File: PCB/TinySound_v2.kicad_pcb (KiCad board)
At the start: 4 copper layers, 15.2 x 20 mm, 35 parts, among them J1 Conn_01x07, J2 USB_B_Micro, J3 Conn_01x07, U1 MIC5504-3.3YMT, U2 MAX98360AEFB+T, U3 RP2040, U4 W25Q128JVS, Y1 12M

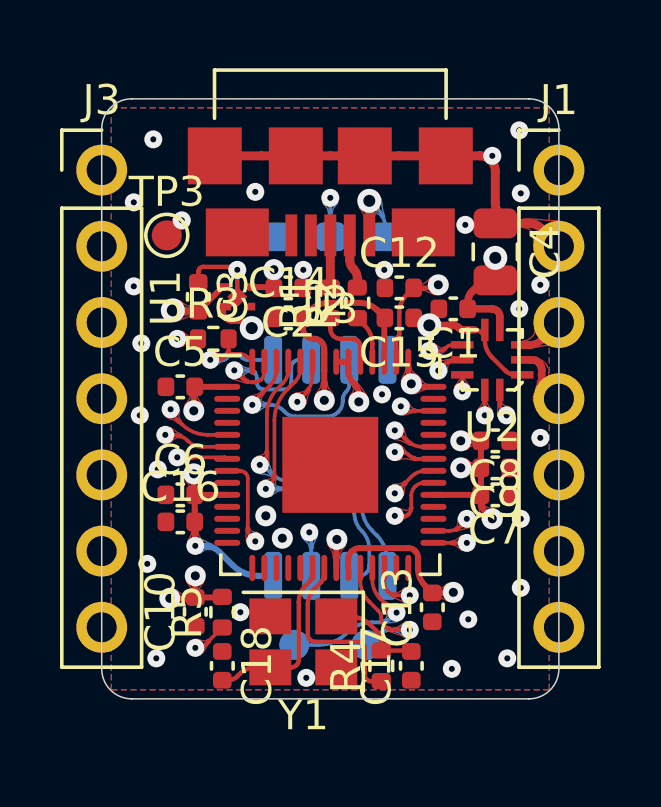
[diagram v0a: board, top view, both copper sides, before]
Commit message: Cleared round traces on PCB, added WS2812 in schematic
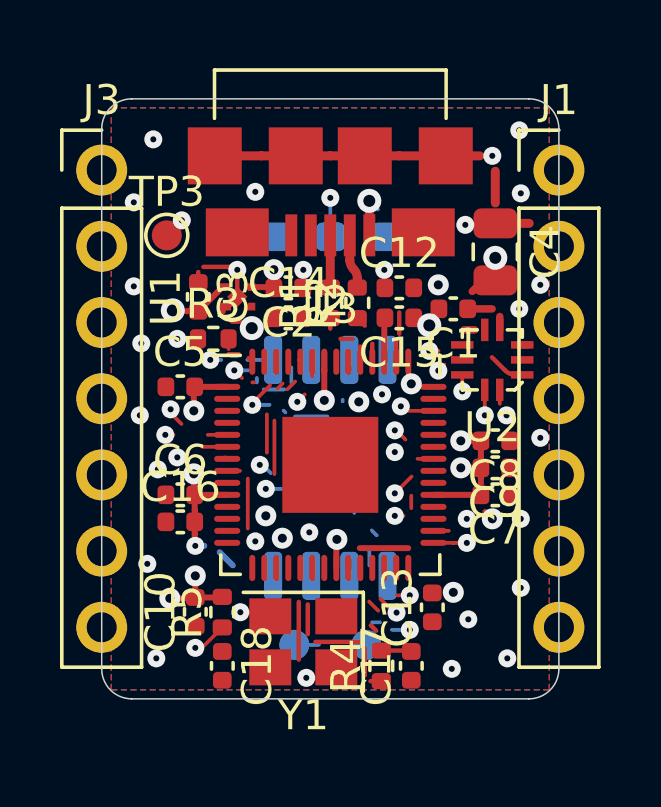
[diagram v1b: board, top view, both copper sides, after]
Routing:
- net +3V3: track 75.3 -> 55.3 mm
- net /+1V1: track 21.1 -> 10.00 mm
- net GND: track 23.2 -> 15.8 mm
- net +5V: track 21.7 -> 14.6 mm
- net /GPIO4: track 11.0 -> 5.33 mm
- net /QSPI_SD0: track 10.4 -> 4.84 mm
- net /RUN: track 14.1 -> 9.32 mm
- net /QSPI_SCLK: track 10.9 -> 6.21 mm
- net /AU_DIN: track 8.66 -> 4.56 mm
- net /QSPI_SD2: track 6.57 -> 2.89 mm
- net /SWCLK: track 4.67 -> 1.03 mm
- net /SWDIO: track 5.53 -> 1.91 mm
- net /AU_GAIN: track 9.55 -> 6.37 mm
- net /BOOTSEL: track 6.27 -> 3.19 mm
- net /QSPI_SD3: track 7.46 -> 4.50 mm
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
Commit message: New component arrangement vor v2.1
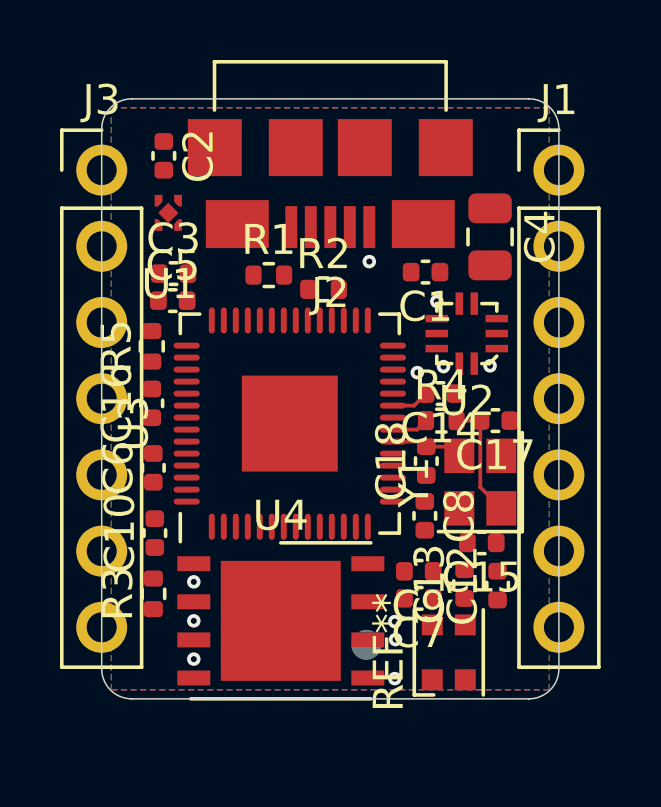
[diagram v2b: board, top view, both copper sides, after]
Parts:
- removed R6, R7: 100k, Resistor_SMD:R_0603_1608Metric_Pad0.98x0.95mm_HandSolder
- removed TP3: TestPoint, TestPoint:TestPoint_Pad_D1.0mm
- added REF**: LED_WS2812B-2020_PLCC4_2.0x2.0mm, LED_SMD:LED_WS2812B-2020_PLCC4_2.0x2.0mm, F.Cu at (104.0, 120.0)
- U4: footprint Package_SO:SOIC-8_5.23x5.23mm_P1.27mm -> Package_DFN_QFN:DFN-8-1EP_6x5mm_P1.27mm_EP4x4mm; moved to F.Cu
- Y1: footprint Crystal:Crystal_SMD_3225-4Pin_3.2x2.5mm -> Crystal:Crystal_SMD_2520-4Pin_2.5x2.0mm
- moved C12 10.5 mm to (105.6, 117.7), turned to 90 degrees
- moved C18 9.63 mm to (103.2, 113.6), turned to 90 degrees
- moved R5 9.17 mm to (94.0, 109.8)
- moved R3 8.73 mm to (94.1, 118.0), turned to 90 degrees
- moved C17 8.64 mm to (105.5, 112.2), turned to 180 degrees
- moved R4 8.42 mm to (103.7, 112.2), turned to 0 degrees
- moved C15 7.99 mm to (105.0, 116.3)
- moved Y1 7.95 mm to (105.0, 114.3), turned to 90 degrees
- moved C2 6.05 mm to (94.5, 103.4), turned to -90 degrees
- moved C14 5.67 mm to (103.7, 111.3), turned to 180 degrees
- moved U4 5.36 mm to (98.3, 118.9), turned to 0 degrees
- moved C7 4.29 mm to (103.0, 118.2)
- moved C9 4.29 mm to (103.0, 117.2)
- moved C16 4.06 mm to (94.0, 111.7), turned to 90 degrees
- moved U1 3.62 mm to (94.6, 105.3), turned to 0 degrees
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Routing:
- net +3V3: track 55.3 -> 0.00 mm, vias 13 -> 0
- net GND: track 15.8 -> 0.00 mm, vias 31 -> 7
- net +5V: track 14.6 -> 0.00 mm, vias 3 -> 0
- net /GPIO3: track 11.1 -> 0.00 mm, vias 1 -> 0
- net /RUN: track 9.32 -> 0.00 mm, vias 2 -> 0
- net /+1V1: track 10.00 -> 1.27 mm, vias 2 -> 1
- net /AU_GAIN: track 6.37 -> 0.00 mm, vias 2 -> 0
- net /QSPI_SCLK: track 6.21 -> 0.00 mm, vias 1 -> 0
- net /GPIO4: track 5.33 -> 0.00 mm, vias 1 -> 0
- net /AU_LRCLK: track 4.88 -> 0.00 mm, vias 2 -> 1
- net /QSPI_SD0: track 4.84 -> 0.00 mm, vias 1 -> 0
- net /AU_DIN: track 4.56 -> 0.00 mm, vias 2 -> 1
- net /QSPI_SD3: track 4.50 -> 0.00 mm, vias 2 -> 0
- net /AU_BCLK: track 4.16 -> 0.00 mm, vias 2 -> 0
- net /AU_EN: track 4.11 -> 0.00 mm, vias 2 -> 1
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
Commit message: Moved components to better positions
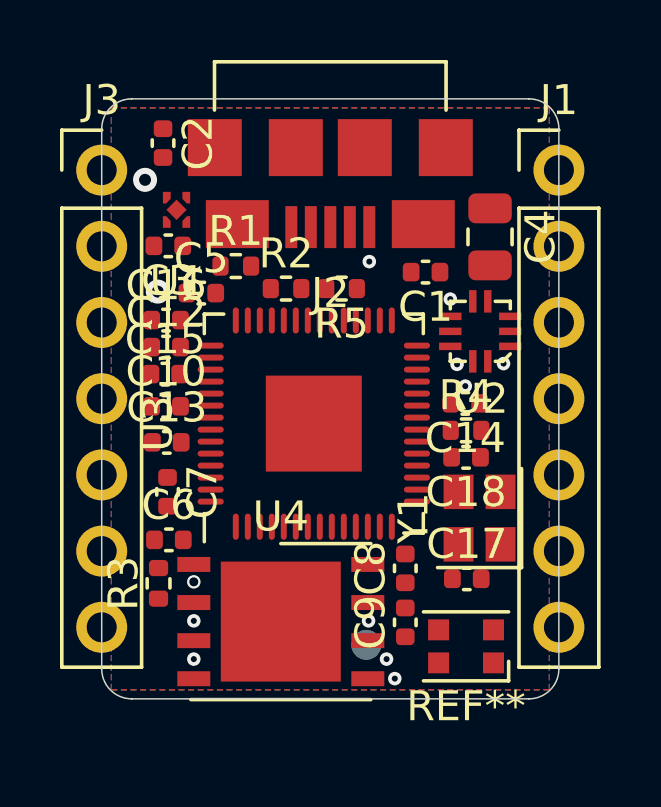
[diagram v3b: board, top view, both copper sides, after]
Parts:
- moved C12 13.6 mm to (94.5, 109.8), turned to 0 degrees
- moved C15 12.0 mm to (94.5, 110.7), turned to 0 degrees
- moved C13 11.0 mm to (94.5, 113.0), turned to 0 degrees
- moved C7 9.10 mm to (94.6, 114.6), turned to -90 degrees
- moved R5 6.61 mm to (100.4, 107.8), turned to 180 degrees
- moved C17 5.36 mm to (104.5, 117.5), turned to 0 degrees
- moved C10 4.24 mm to (94.5, 111.8), turned to 0 degrees
- moved C16 2.82 mm to (94.5, 108.9), turned to 0 degrees
- moved C6 2.46 mm to (94.6, 116.2), turned to 0 degrees
- moved C8 1.87 mm to (102.5, 117.2), turned to 90 degrees
- moved C9 1.76 mm to (102.5, 119.0), turned to 90 degrees
- moved C18 1.33 mm to (104.5, 113.5), turned to 180 degrees
- moved R2 1.25 mm to (98.5, 107.8)
- moved Y1 1.20 mm to (105.0, 115.5)
- moved R1 1.14 mm to (96.8, 107.1)
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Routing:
- net Net-(C17-Pad2): track 4.04 -> 0.00 mm
- net /XIN: track 2.41 -> 0.00 mm
- net /+1V1: track 1.27 -> 0.00 mm
- net /XOUT: track 1.23 -> 0.00 mm
- net GND: vias 7 -> 8
- net +3V3: vias 0 -> 1
